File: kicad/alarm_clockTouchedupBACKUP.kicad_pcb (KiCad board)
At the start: 2 copper layers, 41 parts, among them M1 2N7000, P3 CONN_02X12, P4 CONN_2, P5 CONN_3, P6 CONN_2, Q1 2N3906, Q2 2N3906, Q3 2N3906, Q4 2N3906, Q5 2N3906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

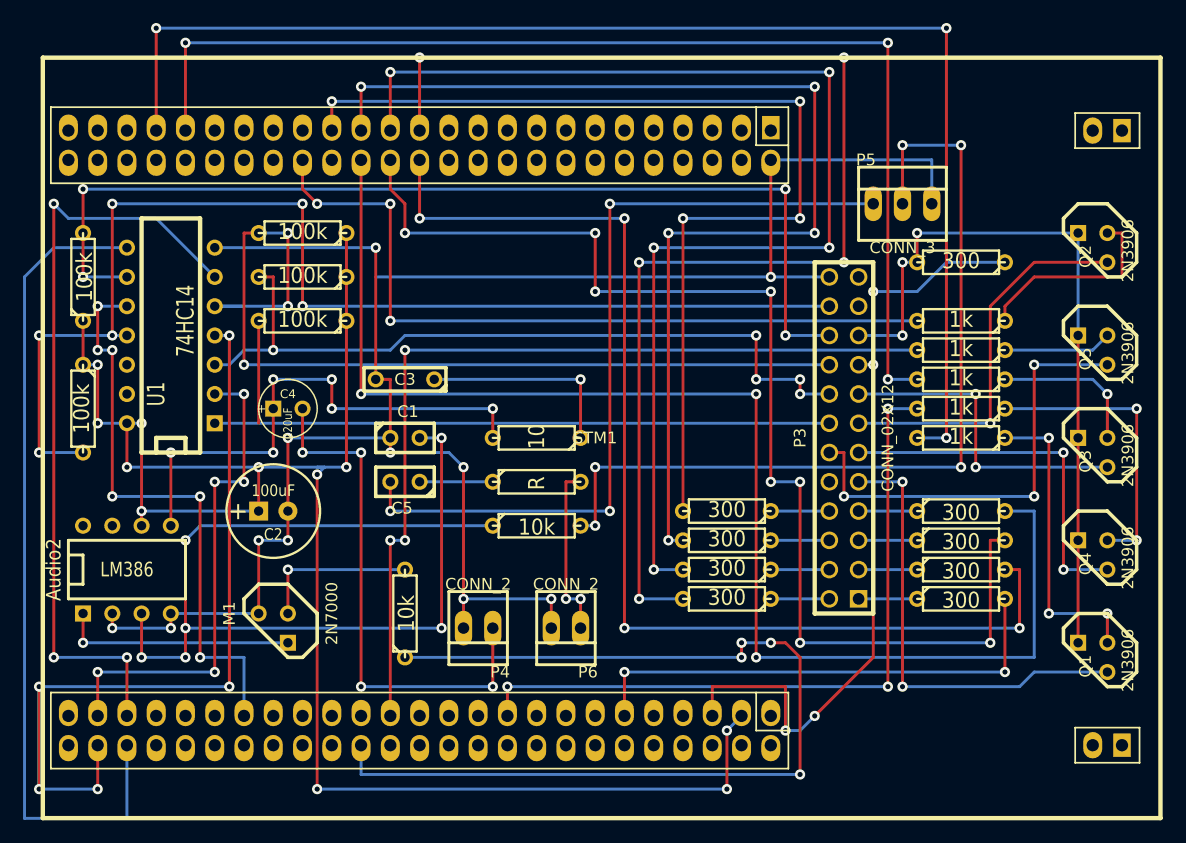
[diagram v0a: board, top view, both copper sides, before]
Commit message: Drill hole sizes fixed
Match APCircuits free sizes

Header holes deleted D:
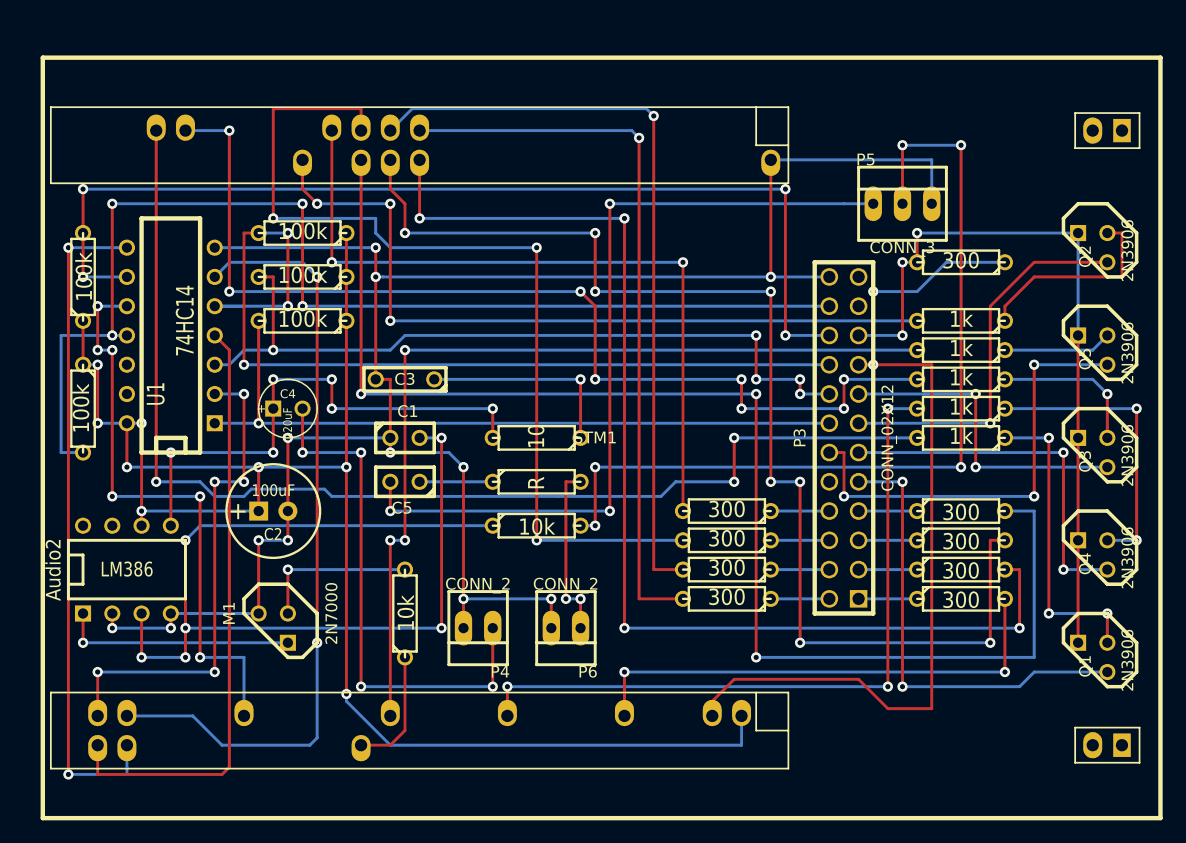
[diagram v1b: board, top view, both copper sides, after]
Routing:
- net PD6: track 86.9 -> 10.7 mm, vias 4 -> 0
- net PE7: track 111.8 -> 63.1 mm, vias 5 -> 1
- net PE9: track 104.1 -> 65.8 mm, vias 5 -> 1
- net PC7: track 83.8 -> 52.2 mm, vias 5 -> 0
- net PE13: track 88.9 -> 63.5 mm, vias 4 -> 2
- net PE11: track 96.5 -> 81.8 mm, vias 5 -> 3
- net PC9: track 72.2 -> 58.4 mm, vias 0 -> 2
- net PD11: track 115.6 -> 101.9 mm
- net 5V_203: track 151.3 -> 138.7 mm, vias 12 -> 9
- net PD9: track 100.3 -> 89.4 mm, vias 3 -> 8
- net 3V_205: track 68.5 -> 78.5 mm, vias 4 -> 2
- net S5: track 105.4 -> 101.6 mm, vias 6 -> 4
- net PC8: track 67.4 -> 67.8 mm, vias 3 -> 2
- net S1: vias 1 -> 2
- net AudioJackGrnd: vias 11 -> 12
